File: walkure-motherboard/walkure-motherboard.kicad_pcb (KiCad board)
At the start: 2 copper layers, 240 x 85 mm, 16 parts, among them J1 Conn_01x02, J2 Conn_01x02, J3 Conn_01x02, J4 Conn_01x02, J5 Conn_01x02, J6 Conn_01x02, J7 Conn_01x02, J8 Conn_01x02, J9 Conn_01x02

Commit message: Walkure motherboard v1.0 schematic
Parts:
- added J10: Conn_01x02, MHCI:2060-452-998-404 Wago, F.Cu at (35.0, 32.0)
- added J11: Conn_01x03, Connector_PinHeader_2.54mm:PinHeader_1x03_P2.54mm_Vertical, F.Cu at (137.2, 30.5)
- added J12: Conn_01x04, Connector_PinHeader_2.54mm:PinHeader_1x04_P2.54mm_Vertical, F.Cu at (160.0, 27.9)
- added J13: Conn_01x04, Connector_PinHeader_2.54mm:PinHeader_1x04_P2.54mm_Vertical, F.Cu at (165.1, 27.9)
- added J14: Conn_01x04, Connector_PinHeader_2.54mm:PinHeader_1x04_P2.54mm_Vertical, F.Cu at (170.2, 27.9)
- added J15: Conn_01x04, Connector_PinHeader_2.54mm:PinHeader_1x04_P2.54mm_Vertical, F.Cu at (175.3, 27.9)
- added J16: Conn_01x04, Connector_PinHeader_2.54mm:PinHeader_1x04_P2.54mm_Vertical, F.Cu at (182.9, 27.9)
- added J17: Conn_01x04, Connector_PinHeader_2.54mm:PinHeader_1x04_P2.54mm_Vertical, F.Cu at (188.0, 27.9)
- added J18: Conn_01x04, Connector_PinHeader_2.54mm:PinHeader_1x04_P2.54mm_Vertical, F.Cu at (195.6, 27.9)
- added J19: Conn_01x04, Connector_PinHeader_2.54mm:PinHeader_1x04_P2.54mm_Vertical, F.Cu at (200.7, 27.9)
- added J20: Conn_01x03, Connector_PinHeader_2.54mm:PinHeader_1x03_P2.54mm_Vertical, F.Cu at (142.2, 30.5)
- added J21: Conn_01x03, Connector_PinHeader_2.54mm:PinHeader_1x03_P2.54mm_Vertical, F.Cu at (147.3, 30.5)
- added J22: Conn_01x03, Connector_PinHeader_2.54mm:PinHeader_1x03_P2.54mm_Vertical, F.Cu at (152.4, 30.5)
- added U10: DS18B20Z, Package_SO:SOIC-8_3.9x4.9mm_P1.27mm, F.Cu at (166.3, 82.0)
- added U11: 74LS04, Package_DIP:DIP-14_W7.62mm_Socket, F.Cu at (60.2, -7.42)
- added U12: TSR_2-2450, Converter_DCDC:Converter_DCDC_TRACO_TSR-1_THT, F.Cu at (58.9, 32.0)
- added U8: ~, MHCI:ESP-32-S3-Zero - PTH, F.Cu at (99.4, 33.0)
- added U9: LTV-827, Package_DIP:DIP-8_W7.62mm_Socket, F.Cu at (45.2, -8.80)
- moved J7 33.9 mm to (35.0, 88.9)
- moved J8 33.9 mm to (35.0, 98.4)
- moved J9 33.9 mm to (35.0, 108.0)
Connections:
- J1 pad 1: /Driver1/LED- -> /Driver1/LED+
- J1 pad 2: /Driver1/LED+ -> /Driver1/LED-
- J2 pad 1: /Driver/LED- -> /Driver/LED+
- J2 pad 2: /Driver/LED+ -> /Driver/LED-
- J3 pad 1: /Driver2/LED- -> /Driver2/LED+
- J3 pad 2: /Driver2/LED+ -> /Driver2/LED-
- J4 pad 1: /Driver3/LED- -> /Driver3/LED+
- J4 pad 2: /Driver3/LED+ -> /Driver3/LED-
- J5 pad 1: /Driver4/LED- -> /Driver4/LED+
- J5 pad 2: /Driver4/LED+ -> /Driver4/LED-
- J6 pad 1: /Driver5/LED- -> /Driver5/LED+
- J6 pad 2: /Driver5/LED+ -> /Driver5/LED-
- J7 pad 2: GND -> GND 1
- J8 pad 2: GND -> GND 2
- J9 pad 2: GND -> GND 3
- U1 pad 2: GND -> GND 1
- U1 pad 3: IO1 -> IO1 ISO
- U2 pad 1: unconnected-(U2-VIN-Pad1) -> +5V
- U2 pad 17: unconnected-(U2-SDA-Pad17) -> SDA
- U2 pad 18: unconnected-(U2-SCL-Pad18) -> SCL
- U2 pad 19: unconnected-(U2-RX-Pad19) -> RX
- U2 pad 20: unconnected-(U2-TX-Pad20) -> TX
- U3 pad 2: GND -> GND 1
- U3 pad 3: IO2 -> IO2 ISO
- U4 pad 2: GND -> GND 2
- U4 pad 3: IO3 -> IO3 ISO
- U5 pad 2: GND -> GND 2
- U5 pad 3: IO4 -> IO4 ISO
- U6 pad 2: GND -> GND 3
- U6 pad 3: IO5 -> IO5 ISO
- U7 pad 2: GND -> GND 3
- U7 pad 3: IO6 -> IO6 ISO
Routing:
- net VCC 1: track 0.00 -> 187.3 mm
- net VCC 2: track 0.00 -> 178.7 mm
- net VCC 3: track 0.00 -> 168.3 mm
- net /Driver2/LED-: track 0.00 -> 111.3 mm
- net /Driver/LED-: track 0.00 -> 111.3 mm
- net /Driver4/LED-: track 0.00 -> 102.0 mm
- net /Driver2/LED+: track 0.00 -> 102.0 mm
- net /Driver/LED+: track 0.00 -> 102.0 mm
- net /Driver4/LED+: track 0.00 -> 92.7 mm
- net GND 2: track 0.00 -> 78.2 mm
- net GND 3: track 0.00 -> 78.2 mm
- net GND 1: track 0.00 -> 78.2 mm
- net /Driver3/LED-: track 0.00 -> 43.5 mm
- net /Driver1/LED-: track 0.00 -> 43.5 mm
- net /Driver5/LED-: track 0.00 -> 34.2 mm
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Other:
- board size 240 x 85 mm -> 240 x 100 mm

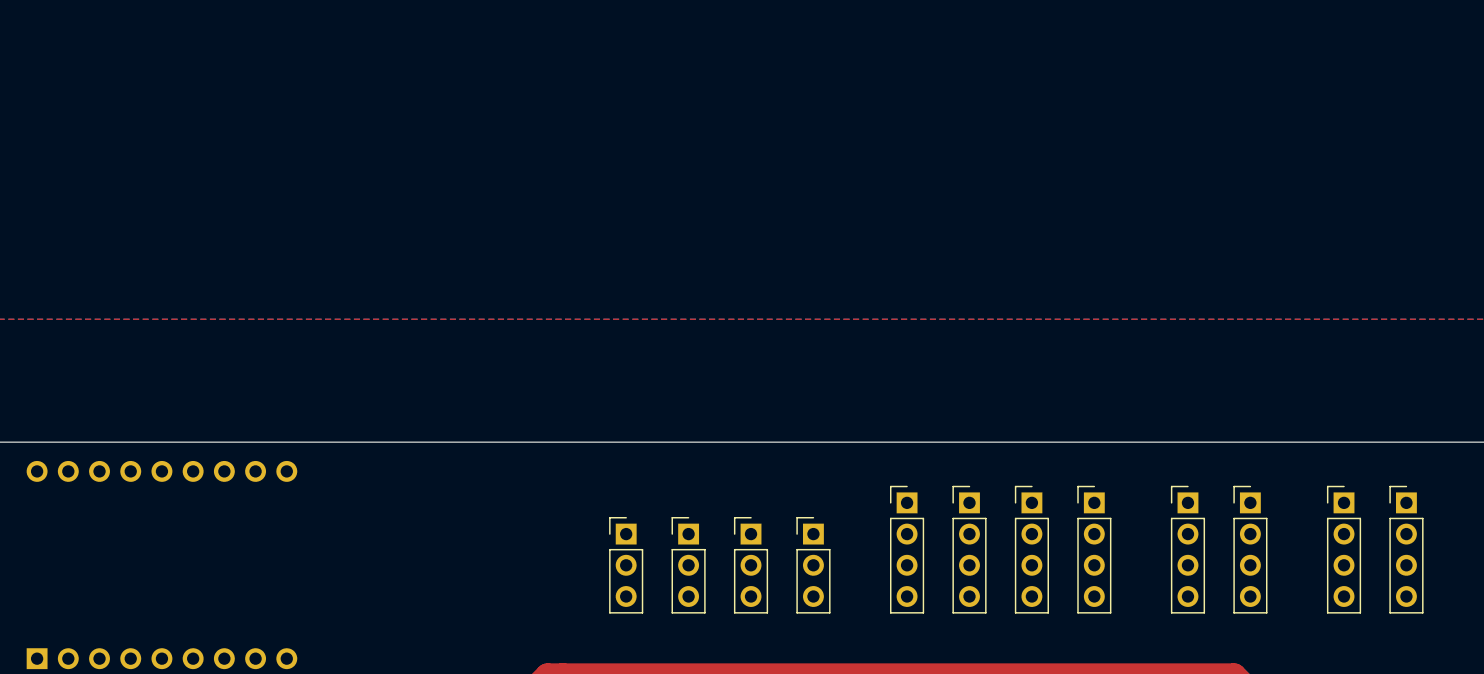
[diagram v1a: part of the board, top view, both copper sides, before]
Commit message: Adding fans and breakouts
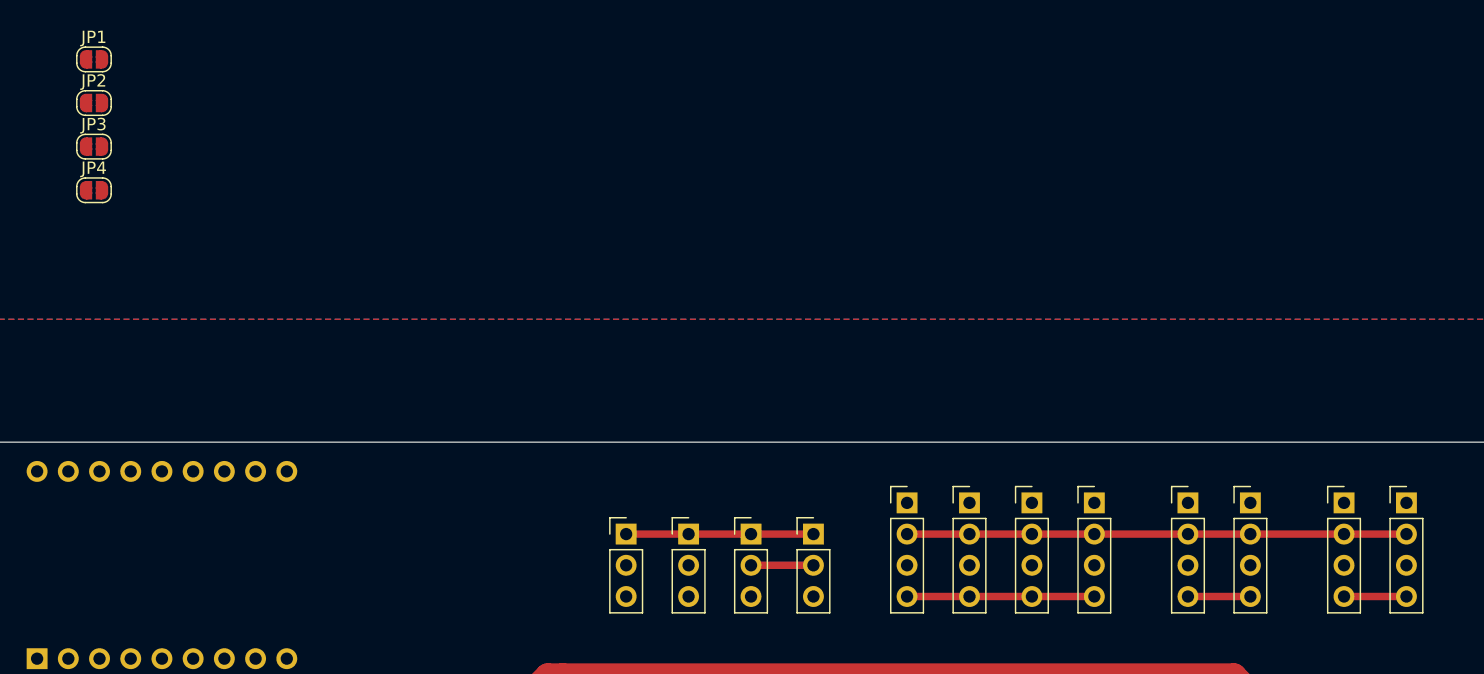
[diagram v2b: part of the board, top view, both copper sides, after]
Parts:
- added JP1: SolderJumper_2_Open, Jumper:SolderJumper-2_P1.3mm_Open_RoundedPad1.0x1.5mm, F.Cu at (93.8, -8.15)
- added JP2: SolderJumper_2_Open, Jumper:SolderJumper-2_P1.3mm_Open_RoundedPad1.0x1.5mm, F.Cu at (93.8, -4.60)
- added JP3: SolderJumper_2_Open, Jumper:SolderJumper-2_P1.3mm_Open_RoundedPad1.0x1.5mm, F.Cu at (93.8, -1.05)
- added JP4: SolderJumper_2_Open, Jumper:SolderJumper-2_P1.3mm_Open_RoundedPad1.0x1.5mm, F.Cu at (93.8, 2.50)
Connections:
- J10 pad 2: GND -> GND 1
- J11 pad 3: GND -> GND 1
- J12 pad 1: GND -> GND 1
- J13 pad 1: GND -> GND 1
- J14 pad 1: GND -> GND 1
- J15 pad 1: GND -> GND 1
- J16 pad 1: GND -> GND 1
- J17 pad 1: GND -> GND 1
- J18 pad 1: GND -> GND 1
- J19 pad 1: GND -> GND 1
- J20 pad 3: GND -> GND 1
- J21 pad 3: GND -> GND 1
- J22 pad 3: GND -> GND 1
- J8 pad 2: GND 2 -> GND 1
- J9 pad 2: GND 3 -> GND 1
- U10 pad 5: GND -> GND 1
- U12 pad 2: GND -> GND 1
- U2 pad 10: GND -> GND 1
- U2 pad 3: unconnected-(U2-5V-Pad3) -> +5V
- U2 pad 4: unconnected-(U2-5V-Pad4) -> +5V
- U2 pad 5: unconnected-(U2-5V-Pad5) -> +5V
- U2 pad 6: unconnected-(U2-5V-Pad6) -> +5V
- U2 pad 7: GND -> GND 1
- U2 pad 8: GND -> GND 1
- U2 pad 9: GND -> GND 1
- U4 pad 2: GND 2 -> GND 1
- U5 pad 2: GND 2 -> GND 1
- U6 pad 2: GND 3 -> GND 1
- U7 pad 2: GND 3 -> GND 1
- U8 pad 1: unconnected-(U8-GPIO1-Pad1) -> Net-(JP1-B)
- U8 pad 2: unconnected-(U8-GPIO2-Pad2) -> Net-(JP2-B)
- U8 pad GND: GND -> GND 1
- U8 pad RX: unconnected-(U8-PadRX) -> Net-(JP4-A)
- U8 pad TX: unconnected-(U8-PadTX) -> Net-(JP3-A)
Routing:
- net GND 1: track 78.2 -> 234.5 mm
- net GND 2: track 78.2 -> 0.00 mm
- net GND 3: track 78.2 -> 0.00 mm
- net +12V: track 0.00 -> 40.6 mm
- net +3V3: track 0.00 -> 15.2 mm
- net FAN1: track 0.00 -> 15.2 mm
- net TEMP2: track 0.00 -> 5.08 mm
- net FAN3: track 0.00 -> 5.08 mm
- net FAN2: track 0.00 -> 5.08 mm
- added copper zone on B.Cu, net GND 1
- added copper zone on F.Cu, net GND 1
- removed copper zone on B.Cu, net GND
- removed copper zone on F.Cu, net GND

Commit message: Walkure motherboard production v1.0
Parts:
- removed U11: 74LS04, Package_DIP:DIP-14_W7.62mm_Socket
- removed U12: TSR_2-2450, Converter_DCDC:Converter_DCDC_TRACO_TSR-1_THT
- removed U9: LTV-827, Package_DIP:DIP-8_W7.62mm_Socket
- added ?: , , F.Cu at (200.7, 27.9)
- added D1: D_Schottky, Diode_THT:D_DO-41_SOD81_P5.08mm_Vertical_AnodeUp, F.Cu at (156.2, 33.0)
- added D2: D_Schottky, Diode_THT:D_DO-41_SOD81_P5.08mm_Vertical_AnodeUp, F.Cu at (179.1, 33.0)
- added D3: D_Schottky, Diode_THT:D_DO-41_SOD81_P5.08mm_Vertical_AnodeUp, F.Cu at (191.8, 33.1)
- added F1: Fuse, MHCI:Keystone 4628, F.Cu at (57.1, 32.0)
- added H1: MountingHole, MountingHole:MountingHole_3.2mm_M3_ISO14580, F.Cu at (55.0, 55.0)
- added H2: MountingHole, MountingHole:MountingHole_3.2mm_M3_ISO14580, F.Cu at (141.0, 55.0)
- added H3: MountingHole, MountingHole:MountingHole_3.2mm_M3_ISO14580, F.Cu at (227.0, 55.0)
- added H4: MountingHole, MountingHole:MountingHole_3.2mm_M3_ISO14580, F.Cu at (227.0, 109.0)
- added H5: MountingHole, MountingHole:MountingHole_3.2mm_M3_ISO14580, F.Cu at (55.0, 109.0)
- added H6: MountingHole, MountingHole:MountingHole_3.2mm_M3_ISO14580, F.Cu at (141.0, 109.0)
- added JP5: SolderJumper_3_Open, Jumper:SolderJumper-3_P1.3mm_Open_RoundedPad1.0x1.5mm, F.Cu at (106.7, 47.7)
- added JP6: SolderJumper_2_Open, Jumper:SolderJumper-2_P1.3mm_Open_RoundedPad1.0x1.5mm, B.Cu at (106.8, 46.9)
- added JP7: SolderJumper_2_Open, Jumper:SolderJumper-2_P1.3mm_Open_RoundedPad1.0x1.5mm, B.Cu at (114.5, 47.0)
- added JP8: SolderJumper_2_Open, Jumper:SolderJumper-2_P1.3mm_Open_RoundedPad1.0x1.5mm, F.Cu at (101.6, 37.5)
- added JP9: SolderJumper_2_Open, Jumper:SolderJumper-2_P1.3mm_Open_RoundedPad1.0x1.5mm, F.Cu at (104.9, 110.9)
- added TP1: TestPoint, TestPoint:TestPoint_Pad_D2.0mm, F.Cu at (69.5, 39.0)
- added TP14: TestPoint, TestPoint:TestPoint_Pad_D2.0mm, F.Cu at (156.2, 36.8)
- added TP15: TestPoint, TestPoint:TestPoint_Pad_D2.0mm, F.Cu at (179.1, 36.8)
- added TP16: TestPoint, TestPoint:TestPoint_Pad_D2.0mm, F.Cu at (191.8, 36.8)
- added TP17: TestPoint, TestPoint:TestPoint_Pad_D2.0mm, F.Cu at (130.8, 34.3)
- added TP18: TestPoint, TestPoint:TestPoint_Pad_D2.0mm, F.Cu at (143.6, 34.4)
- added TP19: TestPoint, TestPoint:TestPoint_Pad_D2.0mm, F.Cu at (205.1, 33.2)
- added TP2: TestPoint, TestPoint:TestPoint_Pad_D2.0mm, F.Cu at (89.0, 39.0)
- added TP24: TestPoint, TestPoint:TestPoint_Pad_D2.0mm, F.Cu at (96.0, 28.5)
- added TP25: TestPoint, TestPoint:TestPoint_Pad_D2.0mm, F.Cu at (96.0, 32.0)
- added TP26: TestPoint, TestPoint:TestPoint_Pad_D2.0mm, F.Cu at (85.8, 39.0)
- added TP27: TestPoint, TestPoint:TestPoint_Pad_D2.0mm, F.Cu at (76.0, 39.0)
- added TP3: TestPoint, TestPoint:TestPoint_Pad_D2.0mm, F.Cu at (79.2, 39.0)
- added TP4: TestPoint, TestPoint:TestPoint_Pad_D2.0mm, F.Cu at (66.2, 39.0)
- added TP5: TestPoint, TestPoint:TestPoint_Pad_D2.0mm, F.Cu at (46.7, 80.5)
- added TP6: TestPoint, TestPoint:TestPoint_Pad_D2.0mm, F.Cu at (46.6, 96.5)
- added TP7: TestPoint, TestPoint:TestPoint_Pad_D2.0mm, F.Cu at (46.7, 106.0)
- added U13: TXB0102DCU, Package_SO:VSSOP-8_2.3x2mm_P0.5mm, F.Cu at (110.5, 47.0)
- moved U10 67.5 mm to (212.0, 32.4)
- moved JP1 53.8 mm to (109.2, 43.4), turned to 90 degrees
- moved JP2 51.2 mm to (111.8, 43.4), turned to 90 degrees
- moved JP3 30.2 mm to (101.6, 28.1), turned to -90 degrees
- moved JP4 27.6 mm to (104.1, 28.1), turned to -90 degrees
- moved J16 12.7 mm to (195.6, 27.9)
- moved J18 12.7 mm to (182.9, 27.9)
- moved J17 12.7 mm to (200.7, 27.9)
- moved J19 12.7 mm to (188.0, 27.9)
- moved U8 12.4 mm to (111.8, 32.8)
- moved J20 3.59 mm to (139.7, 27.9)
- moved J11 3.59 mm to (134.6, 27.9)
- moved J21 2.54 mm to (147.3, 27.9)
- moved J22 2.54 mm to (152.4, 27.9)
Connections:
- J10 pad 1: +12V -> Net-(J10-Pin_1)
- J10 pad 2: GND 1 -> GND
- J11 pad 3: GND 1 -> GND
- J12 pad 1: GND 1 -> GND
- J13 pad 1: GND 1 -> GND
- J14 pad 1: GND 1 -> GND
- J15 pad 1: GND 1 -> GND
- J16 pad 1: GND 1 -> GND
- J17 pad 1: GND 1 -> GND
- J18 pad 1: GND 1 -> GND
- J19 pad 1: GND 1 -> GND
- J20 pad 3: GND 1 -> GND
- J21 pad 3: GND 1 -> GND
- J22 pad 3: GND 1 -> GND
- J7 pad 2: GND 1 -> GND
- J8 pad 2: GND 1 -> GND
- J9 pad 2: GND 1 -> GND
- U1 pad 2: GND 1 -> GND
- U1 pad 3: IO1 ISO -> IO1
- U10 pad 5: GND 1 -> GND
- U2 pad 1: +5V -> +12V
- U2 pad 10: GND 1 -> GND
- U2 pad 17: SDA -> SDA_5
- U2 pad 18: SCL -> SCL_5
- U2 pad 2: unconnected-(U2-GND_IN-Pad2) -> GND
- U2 pad 6: +5V -> unconnected-(U2-5V-Pad6)
- U2 pad 7: GND 1 -> GND
- U2 pad 8: GND 1 -> GND
- U2 pad 9: GND 1 -> GND
- U3 pad 2: GND 1 -> GND
- U3 pad 3: IO2 ISO -> IO2
- U4 pad 2: GND 1 -> GND
- U4 pad 3: IO3 ISO -> IO3
- U5 pad 2: GND 1 -> GND
- U5 pad 3: IO4 ISO -> IO4
- U6 pad 2: GND 1 -> GND
- U6 pad 3: IO5 ISO -> IO5
- U7 pad 2: GND 1 -> GND
- U7 pad 3: IO6 ISO -> IO6
- U8 pad 4: unconnected-(U8-GPIO4-Pad4) -> FAN1
- U8 pad 5: unconnected-(U8-GPIO5-Pad5) -> FAN2
- U8 pad 5V: +5V -> Net-(JP8-A)
- U8 pad 6: unconnected-(U8-GPIO6-Pad6) -> FAN3
- U8 pad 7: unconnected-(U8-GPIO7-Pad7) -> TEMP1
- U8 pad 8: unconnected-(U8-GPIO8-Pad8) -> TEMP2
- U8 pad 9: unconnected-(U8-GPIO9-Pad9) -> TEMP3
- U8 pad GND: GND 1 -> GND
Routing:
- net +12V: track 40.6 -> 361.2 mm
- net GND: track 0.00 -> 245.1 mm, vias 0 -> 174
- net GND 1: track 234.5 -> 0.00 mm
- net +3V3: track 15.2 -> 246.4 mm, vias 0 -> 2
- net +5V: track 0.00 -> 117.1 mm, vias 0 -> 1
- net TEMP3: track 0.00 -> 112.6 mm
- net IO6: track 0.00 -> 110.1 mm
- net IO2: track 0.00 -> 107.7 mm
- net IO4: track 0.00 -> 101.0 mm
- net FAN3: track 5.08 -> 85.6 mm
- net FAN2: track 5.08 -> 75.4 mm
- net FAN1: track 15.2 -> 65.3 mm
- net IO1: track 0.00 -> 47.6 mm
- net IO5: track 0.00 -> 47.2 mm
- net IO3: track 0.00 -> 38.1 mm
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- added copper zone on B.Cu, net GND
- added copper zone on F.Cu, net GND
- removed copper zone on B.Cu, net GND 1
- removed copper zone on F.Cu, net GND 1
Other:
- outline, holes or cut-outs redrawn
- board text added: "+"
- board text added: "-"
- board text added: "12V"
- board text added: "3V3"
- board text added: "48V"
- board text added: "Array 1"
- board text added: "Array 2"
- board text added: "Array 3"
- board text added: "Array 4"
- board text added: "Array 5"
- board text added: "Array 6"
- board text added: "Aux ESP32"
- board text added: "DATA"
- board text added: "DMX Control Board"
- board text added: "Driver 1"
- board text added: "Driver 2"
- board text added: "Driver 3"
- board text added: "Driver 4"
- board text added: "Driver 5"
- board text added: "Driver 6"
- board text added: "Fan 1"
- board text added: "Fan 2"
- board text added: "Fan 3"
- board text added: "Fuse Holder"
- board text added: "GND"
- board text added: "Lighting Systems Walkure Driver Control v1.0"
- board text added: "PWM"
- board text added: "Temp 1"
- board text added: "Temp 2"
- board text added: "Temp 3"
